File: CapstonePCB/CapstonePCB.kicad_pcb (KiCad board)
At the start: 2 copper layers, 44 parts, among them J1 Conn_02x40_Counter_Clockwise, J2 Barrel_Jack, J3 512964594, SW1 SW_Push, SW2 SW_Push, SW3 SW_Push, U1 NUCLEO64-F411RE, U10 BH1750FVI-TR, U2 LP-MSPM0G3507, U3 STSPIN220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

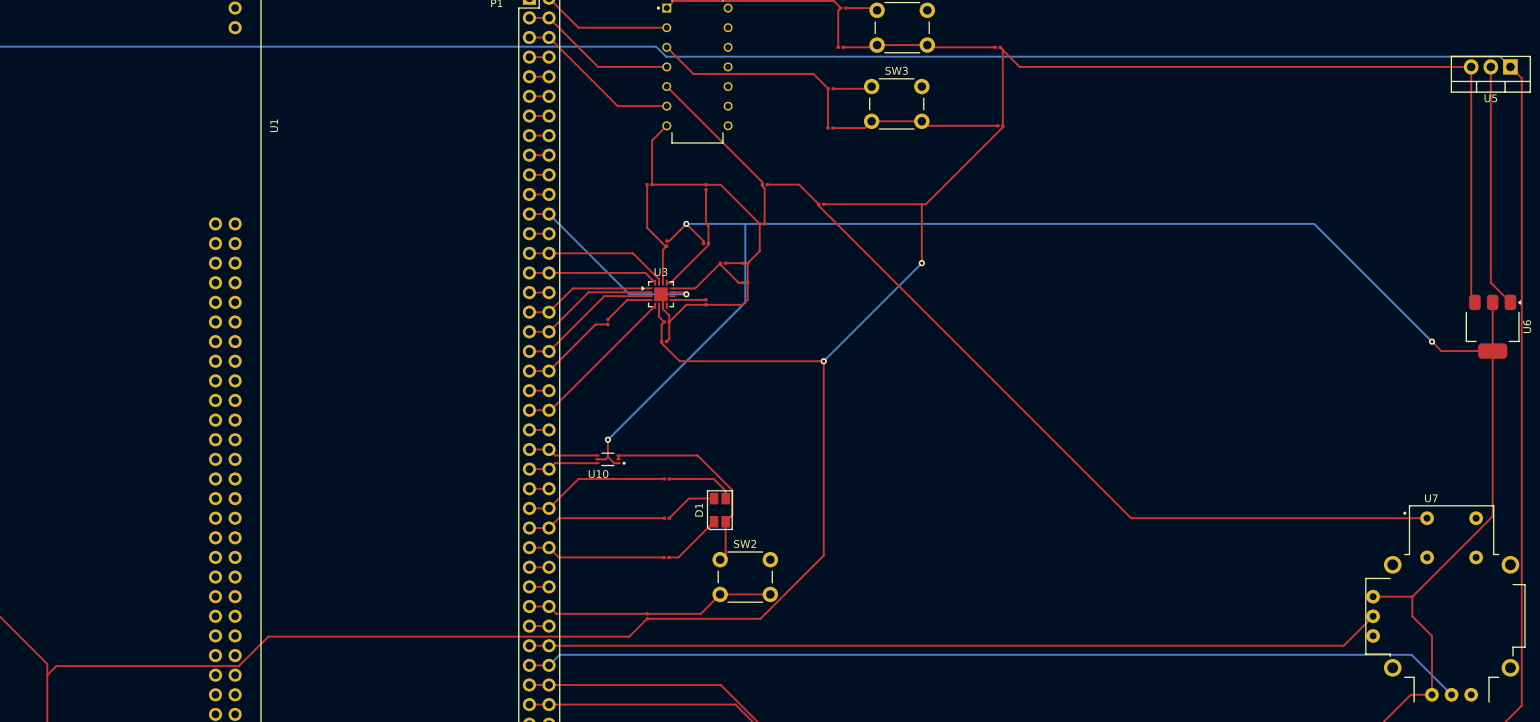
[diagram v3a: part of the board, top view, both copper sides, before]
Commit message: Changed buttons to use 3.3V logic
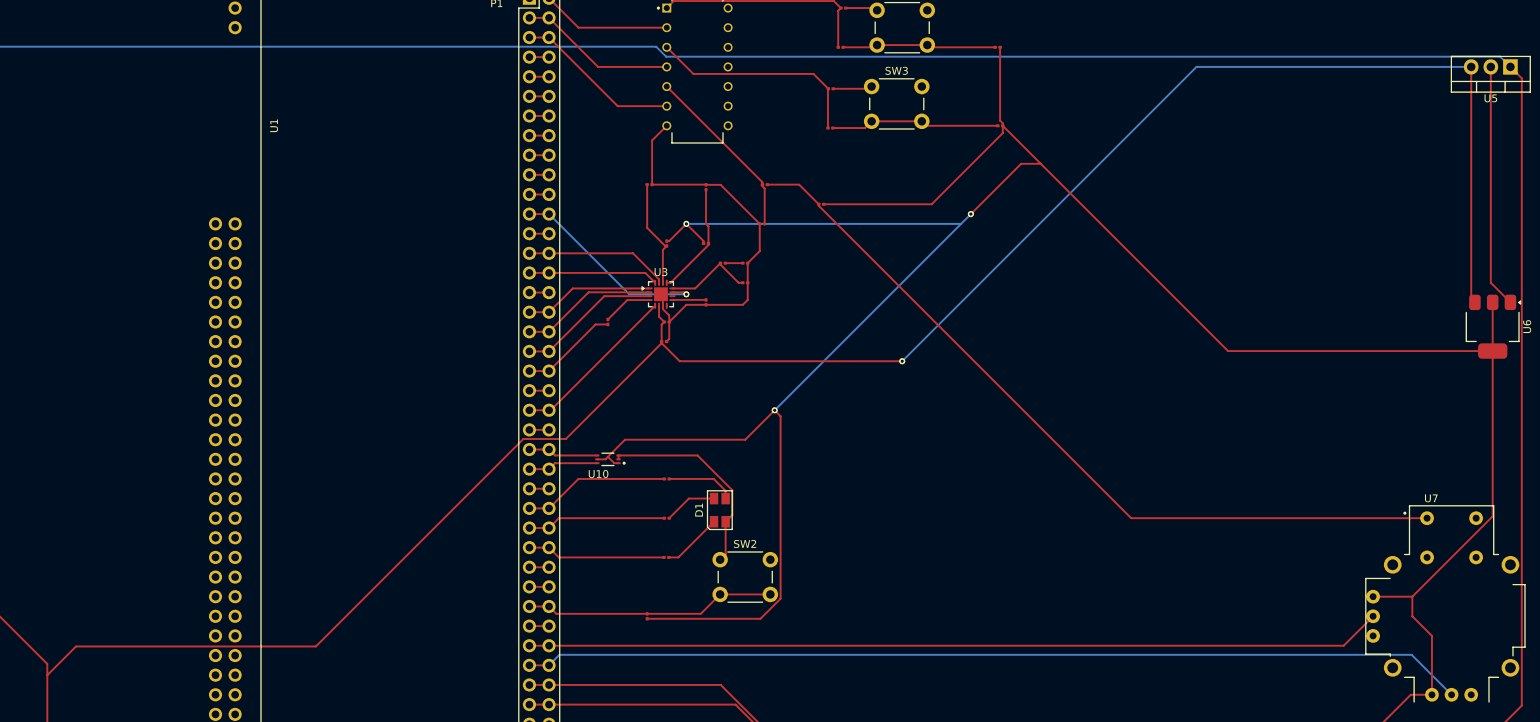
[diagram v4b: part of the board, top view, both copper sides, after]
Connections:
- PullUpResistor2 pad 2: +5V -> VDD
- PullUpResistorJS1 pad 2: +5V -> VDD
- PullUpResistorSW1 pad 2: +5V -> VDD
- PullUpResistorSW3 pad 2: +5V -> VDD
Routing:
- net VDD: track 287.9 -> 403.3 mm
- net +5V: track 407.4 -> 346.8 mm, vias 2 -> 1
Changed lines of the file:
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@@
 			(layers "F.Cu" "F.Mask")
 			(roundrect_rratio 0.25)
-			(net 143 "+5V")
+			(net 172 "VDD")
 			(pintype "passive")
 		)
@@
 			(layers "F.Cu" "F.Mask")
 			(roundrect_rratio 0.25)
-			(net 143 "+5V")
+			(net 172 "VDD")
 			(pintype "passive")
 		)
@@
 			(layers "F.Cu" "F.Mask")
 			(roundrect_rratio 0.25)
-			(net 143 "+5V")
+			(net 172 "VDD")
 			(pintype "passive")
 		)
@@
 			(layers "F.Cu" "F.Mask")
 			(roundrect_rratio 0.25)
-			(net 143 "+5V")
+			(net 172 "VDD")
 			(pintype "passive")
 		)
@@
 	)
 	(segment
-		(start 164.435 60.96)
-		(end 164.435 61.159999)
+		(start 88.622 100.424)
+		(end 84.906 104.14)
 		(width 0.25)
 		(layer "F.Cu")
@@
 	)
 	(segment
-		(start 84.906 102.686)
-		(end 48.26 66.04)
+		(start 152.028999 73.566)
+		(end 146.537116 73.566)
 		(width 0.25)
 		(layer "F.Cu")
@@
 	)
 	(segment
-		(start 198.12 50.8)
-		(end 198.12 43.18)
+		(start 84.906 102.686)
+		(end 48.26 66.04)
 		(width 0.25)
 		(layer "F.Cu")
@@
 	)
 	(segment
-		(start 164.435 61.159999)
-		(end 166.775001 63.5)
-		(width 0.25)
-		(layer "F.Cu")
-		(net 143)
-	)
-	(segment
 		(start 269.24 25.4)
 		(end 269.24 55.4)
@@
 	)
 	(segment
-		(start 86.082 102.964)
-		(end 84.906 104.14)
-		(width 0.25)
-		(layer "F.Cu")
-		(net 143)
-	)
-	(segment
-		(start 198.639999 43.18)
-		(end 198.12 43.18)
+		(start 164.435 61.159999)
+		(end 152.028999 73.566)
 		(width 0.25)
 		(layer "F.Cu")
@@
 	)
 	(segment
-		(start 160.246 99.154)
-		(end 113.517116 99.154)
-		(width 0.25)
-		(layer "F.Cu")
-		(net 143)
-	)
-	(segment
-		(start 198.12 43.18)
-		(end 185.42 43.18)
-		(width 0.25)
-		(layer "F.Cu")
-		(net 143)
-	)
-	(segment
-		(start 185.42 88.655248)
-		(end 177.235248 96.84)
-		(width 0.25)
-		(layer "F.Cu")
-		(net 143)
-	)
-	(segment
-		(start 210.795 25.4)
-		(end 208.255 22.86)
-		(width 0.25)
-		(layer "F.Cu")
-		(net 143)
-	)
-	(segment
-		(start 113.517116 99.154)
-		(end 109.707116 102.964)
+		(start 195.58 63.5)
+		(end 166.775001 63.5)
 		(width 0.25)
 		(layer "F.Cu")
@@
 	)
 	(segment
-		(start 208.6 33.02)
-		(end 208.6 33.219999)
+		(start 146.537116 73.566)
+		(end 119.679116 100.424)
 		(width 0.25)
 		(layer "F.Cu")
@@
 	)
 	(segment
-		(start 109.707116 102.964)
-		(end 86.082 102.964)
-		(width 0.25)
-		(layer "F.Cu")
-		(net 143)
-	)
-	(segment
-		(start 185.42 63.5)
-		(end 185.42 88.655248)
-		(width 0.25)
-		(layer "F.Cu")
-		(net 143)
-	)
-	(segment
-		(start 177.235248 96.84)
-		(end 162.56 96.84)
-		(width 0.25)
-		(layer "F.Cu")
-		(net 143)
-	)
-	(segment
 		(start 86.36 142.24)
 		(end 84.906 140.786)
@@
 	)
 	(segment
-		(start 269.24 25.4)
-		(end 210.795 25.4)
-		(width 0.25)
-		(layer "F.Cu")
-		(net 143)
-	)
-	(segment
 		(start 84.906 140.786)
 		(end 84.906 104.14)
@@
 	)
 	(segment
-		(start 208.6 23.205)
-		(end 208.255 22.86)
+		(start 119.679116 100.424)
+		(end 88.622 100.424)
 		(width 0.25)
 		(layer "F.Cu")
@@
 	)
 	(segment
-		(start 208.6 33.02)
-		(end 208.6 23.205)
-		(width 0.25)
-		(layer "F.Cu")
-		(net 143)
-	)
-	(segment
-		(start 162.56 96.84)
-		(end 160.246 99.154)
-		(width 0.25)
-		(layer "F.Cu")
-		(net 143)
-	)
-	(segment
-		(start 208.6 33.219999)
-		(end 198.639999 43.18)
+		(start 164.435 61.159999)
+		(end 164.435 60.96)
 		(width 0.25)
 		(layer "F.Cu")
@@
 	(segment
 		(start 166.775001 63.5)
-		(end 185.42 63.5)
+		(end 164.435 61.159999)
 		(width 0.25)
 		(layer "F.Cu")
@@
 	)
 	(via
-		(at 198.12 50.8)
+		(at 195.58 63.5)
 		(size 0.8)
 		(drill 0.4)
@@
 		(net 143)
 	)
-	(via
-		(at 185.42 63.5)
-		(size 0.8)
-		(drill 0.4)
-		(layers "F.Cu" "B.Cu")
+	(segment
+		(start 269.24 25.4)
+		(end 233.68 25.4)
+		(width 0.25)
+		(layer "B.Cu")
 		(net 143)
 	)
 	(segment
-		(start 185.42 63.5)
-		(end 198.12 50.8)
+		(start 233.68 25.4)
+		(end 195.58 63.5)
 		(width 0.25)
 		(layer "B.Cu")
@@
 	)
 	(segment
+		(start 179.07 69.85)
+		(end 175.26 73.66)
+		(width 0.25)
+		(layer "F.Cu")
+		(net 172)
+	)
+	(segment
+		(start 179.836 70.616)
+		(end 179.836 94.239248)
+		(width 0.25)
+		(layer "F.Cu")
+		(net 172)
+	)
+	(segment
+		(start 208.6 33.97)
+		(end 199.39 43.18)
+		(width 0.25)
+		(layer "F.Cu")
+		(net 172)
+	)
+	(segment
+		(start 208.6 33.02)
+		(end 208.6 32.7)
+		(width 0.25)
+		(layer "F.Cu")
+		(net 172)
+	)
+	(segment
 		(start 169.86 47.94)
 		(end 167.64 45.72)
@@
 	)
 	(segment
-		(start 157.48 73.66)
-		(end 157.48 75.877)
+		(start 208.255 32.355)
+		(end 208.255 22.86)
 		(width 0.25)
 		(layer "F.Cu")
@@
 	)
 	(segment
-		(start 264.16 60.96)
-		(end 265.38 62.18)
+		(start 210.98 37.94)
+		(end 204.47 44.45)
+		(width 0.25)
+		(layer "F.Cu")
+		(net 172)
+	)
+	(segment
+		(start 179.836 94.239248)
+		(end 177.235248 96.84)
+		(width 0.25)
+		(layer "F.Cu")
+		(net 172)
+	)
+	(segment
+		(start 237.76 62.18)
+		(end 213.52 37.94)
 		(width 0.25)
 		(layer "F.Cu")
@@
 	)
 	(segment
+		(start 157.48 75.877)
+		(end 159.697 73.66)
+		(width 0.25)
+		(layer "F.Cu")
+		(net 172)
+	)
+	(segment
 		(start 261.62 96.52)
 		(end 264.16 99.06)
@@
 	)
 	(segment
-		(start 272.02 83.58)
-		(end 261.62 93.98)
+		(start 159.697 73.66)
+		(end 175.26 73.66)
 		(width 0.25)
 		(layer "F.Cu")
@@
 	(segment
 		(start 272.02 62.18)
-		(end 272.02 83.58)
+		(end 237.76 62.18)
 		(width 0.25)
 		(layer "F.Cu")
@@
 	)
 	(segment
-		(start 265.38 62.18)
-		(end 272.02 62.18)
+		(start 213.52 37.94)
+		(end 210.98 37.94)
+		(width 0.25)
+		(layer "F.Cu")
+		(net 172)
+	)
+	(segment
+		(start 199.39 43.18)
+		(end 185.42 43.18)
+		(width 0.25)
+		(layer "F.Cu")
+		(net 172)
+	)
+	(segment
+		(start 272.02 83.58)
+		(end 261.62 93.98)
+		(width 0.25)
+		(layer "F.Cu")
+		(net 172)
+	)
+	(segment
+		(start 272.02 62.18)
+		(end 272.02 83.58)
 		(width 0.25)
 		(layer "F.Cu")
@@
 	)
 	(segment
+		(start 177.235248 96.84)
+		(end 162.56 96.84)
+		(width 0.25)
+		(layer "F.Cu")
+		(net 172)
+	)
+	(segment
+		(start 179.07 69.85)
+		(end 179.836 70.616)
+		(width 0.25)
+		(layer "F.Cu")
+		(net 172)
+	)
+	(segment
 		(start 261.418 106.68)
 		(end 215.9 152.198)
@@
 	)
 	(segment
+		(start 208.6 33.02)
+		(end 208.6 33.97)
+		(width 0.25)
+		(layer "F.Cu")
+		(net 172)
+	)
+	(segment
+		(start 213.52 37.94)
+		(end 208.6 33.02)
+		(width 0.25)
+		(layer "F.Cu")
+		(net 172)
+	)
+	(segment
+		(start 208.6 32.7)
+		(end 208.255 32.355)
+		(width 0.25)
+		(layer "F.Cu")
+		(net 172)
+	)
+	(segment
 		(start 157.48 75.877)
 		(end 158.303 76.7)
@@
 	)
 	(via
-		(at 157.48 73.66)
+		(at 204.47 44.45)
 		(size 0.8)
 		(drill 0.4)
@@
 	)
 	(via
-		(at 167.64 45.72)
+		(at 179.07 69.85)
 		(size 0.8)
 		(drill 0.4)
@@
 	)
 	(via
-		(at 264.16 60.96)
+		(at 167.64 45.72)
 		(size 0.8)
 		(drill 0.4)
@@
 	)
 	(segment
-		(start 175.26 45.72)
-		(end 248.92 45.72)
-		(width 0.25)
-		(layer "B.Cu")
-		(net 172)
-	)
-	(segment
-		(start 175.26 55.88)
-		(end 157.48 73.66)
+		(start 204.47 44.45)
+		(end 203.2 45.72)
 		(width 0.25)
 		(layer "B.Cu")
@@
 	)
 	(segment
-		(start 175.26 45.72)
-		(end 175.26 55.88)
-		(width 0.25)
-		(layer "B.Cu")
-		(net 172)
-	)
-	(segment
-		(start 167.64 45.72)
-		(end 175.26 45.72)
+		(start 203.2 45.72)
+		(end 167.64 45.72)
 		(width 0.25)
 		(layer "B.Cu")
@@
 	)
 	(segment
-		(start 248.92 45.72)
-		(end 264.16 60.96)
+		(start 203.2 45.72)
+		(end 179.07 69.85)
 		(width 0.25)
 		(layer "B.Cu")

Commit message: Added the buzzer driver
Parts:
- added Q1: 2N7000, Package_TO_SOT_THT:TO-92_Inline, F.Cu at (128.3, 108.0)
- added R_BUZ1: 100R, Resistor_SMD:R_0201_0603Metric, F.Cu at (139.7, 97.8)
- added R_BUZ2: 100kR, Resistor_SMD:R_0201_0603Metric, F.Cu at (139.4, 108.0)
- added U8: WST-1205S, WST-1205S.step:WST-1205S, F.Cu at (129.5, 120.6)
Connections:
- net Net-(J1-Pin_65) renamed BuzzerGPIO
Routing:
- net Net-(Q1-G): track 0.00 -> 21.6 mm
- net GNDREF: track 151.3 -> 172.0 mm
- net +5V: track 346.8 -> 357.5 mm
- net Net-(Q1-S): track 0.00 -> 9.42 mm
- net BuzzerGPIO: track 2.54 -> 9.84 mm

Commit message: Corrected edge cuts layer
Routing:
- net Net-(J1-Pin_71): track 89.5 -> 91.3 mm
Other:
- board outline added: 274.3 x 188 mm
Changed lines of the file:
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@@
 		)
+	)
+	(gr_rect
+		(start 11.43 11.43)
+		(end 285.75 199.39)
+		(stroke
+			(width 0.1)
+			(type default)
+		)
+		(fill no)
+		(layer "Edge.Cuts")
 	)
 	(gr_text "P1"
@@
 	)
 	(segment
-		(start 214.9 152.4)
-		(end 214.9 148.22219)
+		(start 149.86 105.41)
+		(end 175.26 105.41)
 		(width 0.25)
 		(layer "F.Cu")
@@
 	)
 	(segment
-		(start 172.08781 105.41)
-		(end 149.86 105.41)
+		(start 214.9 145.05)
+		(end 214.9 152.4)
 		(width 0.25)
 		(layer "F.Cu")
@@
 	)
 	(segment
-		(start 214.9 148.22219)
-		(end 172.08781 105.41)
-		(width 0.25)
-		(layer "F.Cu")
+		(start 175.26 105.41)
+		(end 214.9 145.05)
+		(width 0.25)
+		(layer "F.Cu")

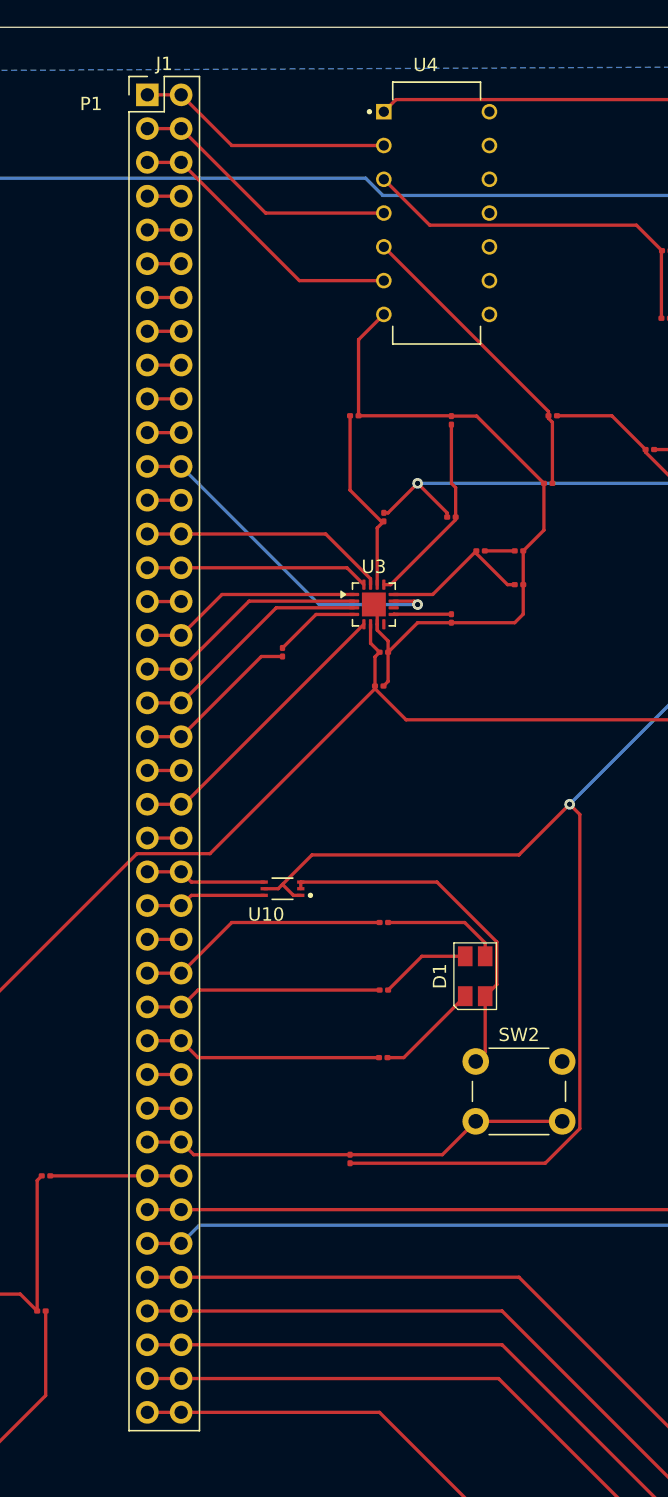
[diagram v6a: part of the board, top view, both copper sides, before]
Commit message: Added pin labels to the silkscreen
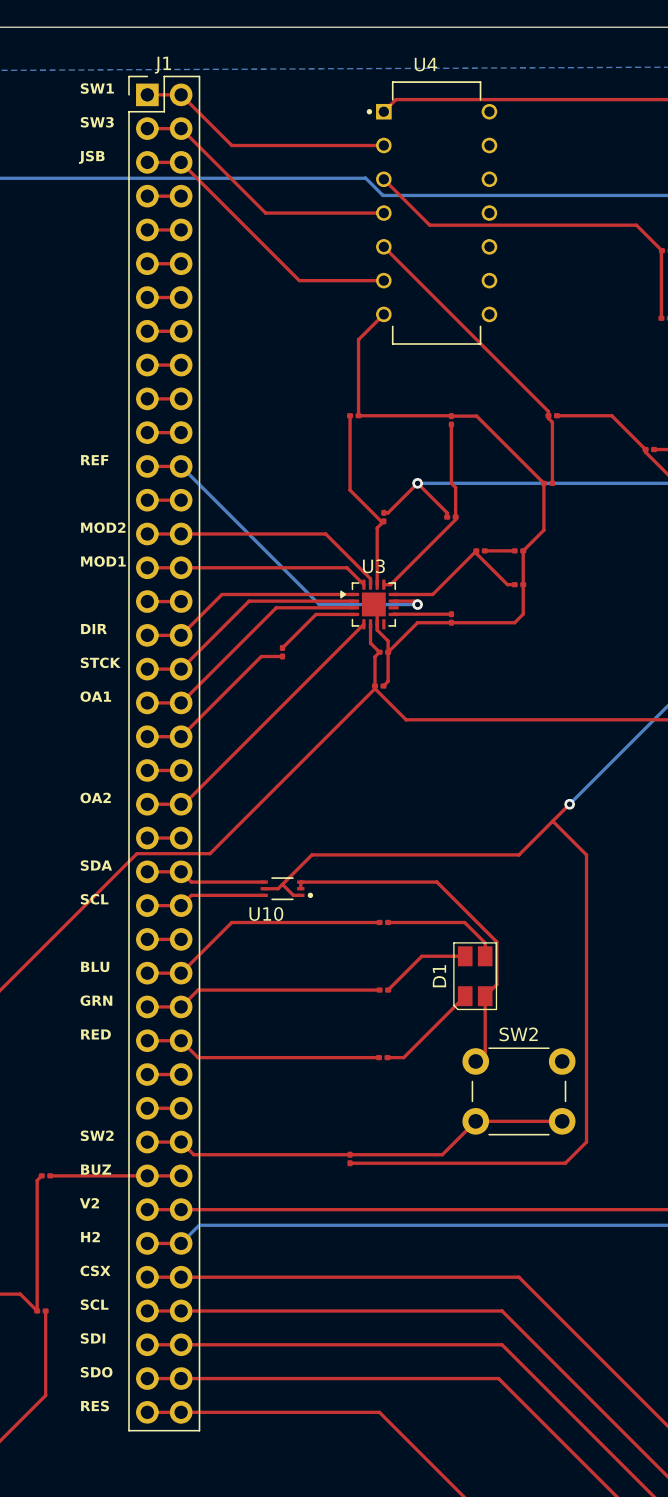
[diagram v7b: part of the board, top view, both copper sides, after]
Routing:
- net VDD: track 403.3 -> 403.9 mm
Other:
- board text added: "BLU"
- board text added: "BUZ"
- board text added: "CSX"
- board text added: "DIR"
- board text added: "GRN"
- board text added: "H2"
- board text added: "JSB"
- board text added: "MOD1"
- board text added: "MOD2"
- board text added: "OA1"
- board text added: "OA2"
- board text added: "RED"
- board text added: "REF"
- board text added: "RES"
- board text added: "SCL"
- board text added: "SDA"
- board text added: "SDI"
- board text added: "SDO"
- board text added: "STCK"
- board text added: "SW1"
- board text added: "SW2"
- board text added: "SW3"
- board text added: "V2"
- board text removed: "P1"
